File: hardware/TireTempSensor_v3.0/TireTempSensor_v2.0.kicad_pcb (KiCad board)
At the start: 4 copper layers, 81.5 x 20.6 mm, 90 parts, among them IC1 TAR5S33UTE85LF, IC2 MLX90621ESF-BAB-000-SP, IC4 TPS54202HDDCR, J1 Conn_01x01, J2 Conn_01x01, J3 FTSH-107-01-L-D-K, J4 Conn_01x01, J5 Conn_01x01, T10 TP_+5V, T14 TP_+3.3V, T15 TP_+2.6V, U1 STM32G0C1KCTxN, U2 MIC5306-2.6YD5-TR, U7 ADM3057ExRW, Y1 ATX-11-F-32.000MHZ-F05-T

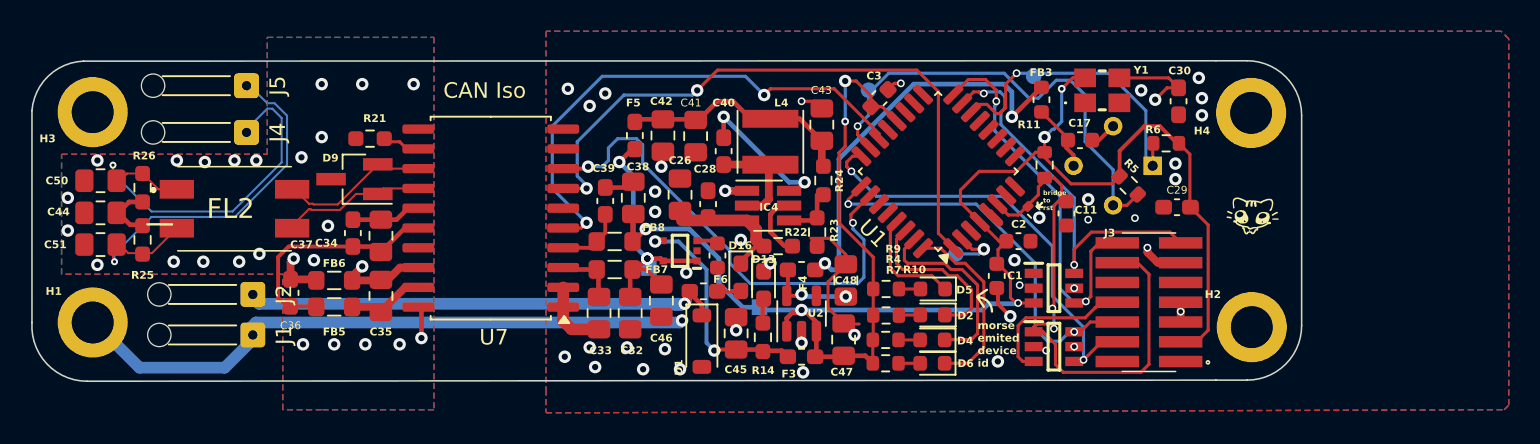
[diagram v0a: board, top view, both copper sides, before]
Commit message: poprawione sciezki; obrocona kamerka tak jak w oryginalne
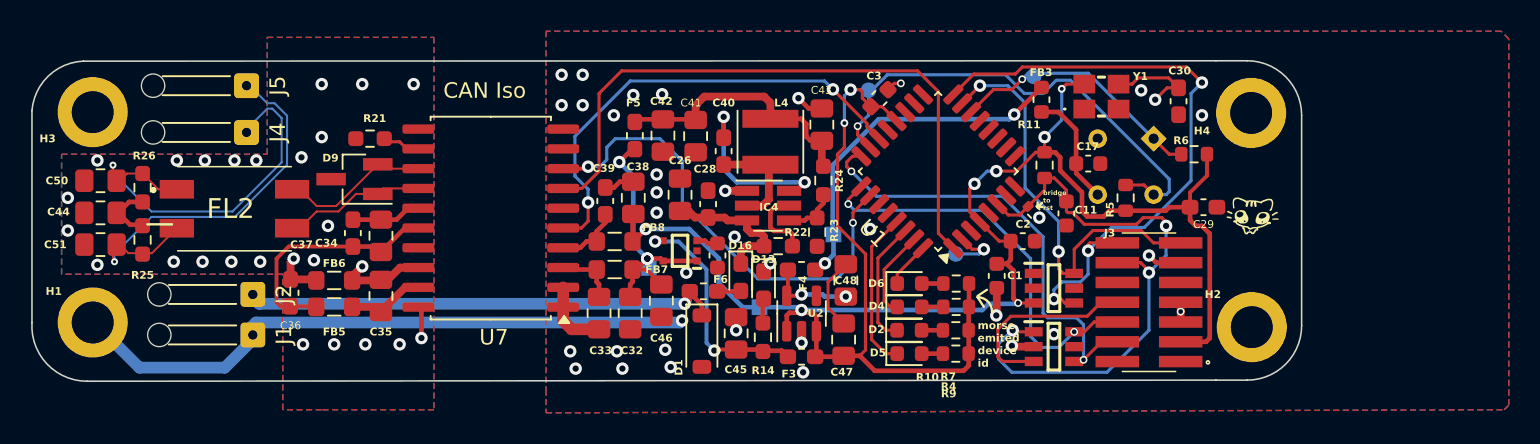
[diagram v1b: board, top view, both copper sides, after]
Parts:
- moved R10 6.84 mm to (148.3, 103.3), turned to 180 degrees
- moved R9 6.10 mm to (148.3, 107.8), turned to 180 degrees
- moved D6 5.33 mm to (145.3, 103.3), turned to 0 degrees
- moved R7 5.00 mm to (148.3, 104.8), turned to 180 degrees
- moved R4 4.57 mm to (148.3, 106.3), turned to 180 degrees
- moved D5 4.41 mm to (145.3, 107.8), turned to 0 degrees
- moved D4 2.58 mm to (145.3, 104.8), turned to 0 degrees
- moved T15 2.09 mm to (140.4, 100.2)
- moved R6 1.93 mm to (163.6, 95.0)
- moved D2 1.79 mm to (145.3, 106.3), turned to 0 degrees
- moved IC2 1.74 mm to (161.0, 94.0), turned to 45 degrees
- moved C29 1.70 mm to (164.2, 98.4), turned to 0 degrees
- moved C17 1.59 mm to (156.8, 95.6)
- moved R5 0.82 mm to (159.2, 97.8), turned to 90 degrees
- moved Y1 0.40 mm to (157.7, 91.3)
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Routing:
- net /URAT_TX: track 23.9 -> 40.6 mm, vias 2 -> 3
- net +3V3: track 112.2 -> 124.4 mm, vias 7 -> 9
- net /LED_ADRESS_INDICATOR_2: track 11.9 -> 2.95 mm
- net /LED_ADRESS_INDICATOR_1: track 12.3 -> 5.74 mm
- net /NRST: track 33.4 -> 39.4 mm, vias 2 -> 3
- net GND: track 69.8 -> 64.0 mm, vias 43 -> 35
- net +2V6: track 25.7 -> 22.0 mm
- net /SWO: track 9.05 -> 12.6 mm
- net /Power Supply 3.3v 2.6v/+5V_OUT: track 13.1 -> 16.5 mm
- net Net-(IC2-VDD): track 4.13 -> 7.44 mm
- net /CAN RX: track 33.2 -> 30.2 mm
- net /LED OK: track 7.34 -> 10.2 mm
- net /LED ERR: track 10.9 -> 8.07 mm
- net /SCL: track 19.0 -> 16.7 mm
- net /Power Supply 3.3v 2.6v/BOOT_+5V: track 9.06 -> 11.0 mm
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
